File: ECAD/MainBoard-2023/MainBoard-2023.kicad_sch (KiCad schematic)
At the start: 71 parts, among them J1 XT60, J10 Conn_01x14, J11 Conn_01x03, J12 Conn_01x04, J13 Conn_01x03, J14 Conn_01x03, J15 Conn_01x03, J16 XT30, J17 XT30, J2 Conn_01x04, J20 BAU, J21 BAU, J22 Conn_01x04, J23 Conn_01x02, J24 Conn_01x07, J26 BAU, J27 BAU, J28 Conn_01x02, J29 Conn_01x02, J3 ConStep1, J30 Conn_01x03, J32 Conn_01x02, J37 Conn_01x02, J38 Conn_01x02, J39 Conn_01x02, J4 Conn_01x02, J40 Conn_01x02, J5 ConStep1, J6 ConStep1, J7 XT30, J8 Conn_01x02, J9 XT60, K1 CB1-P-24V, U1 Teensy3.5_All_Pins, U2 R-78B3.3-2.0, U4 R-78B5.0-2.0

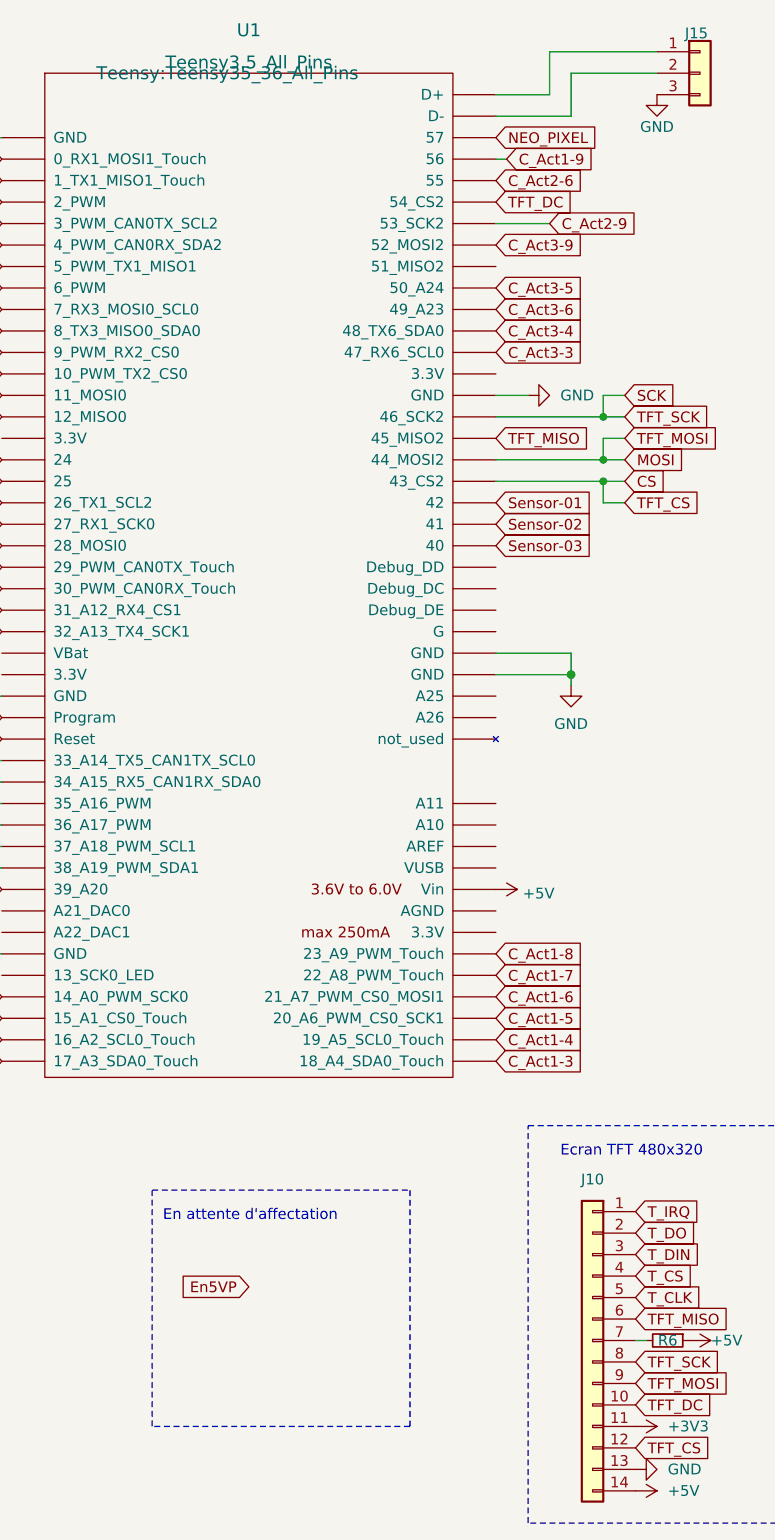
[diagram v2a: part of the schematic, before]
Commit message: clean PCB
Clean routing and DRC errors
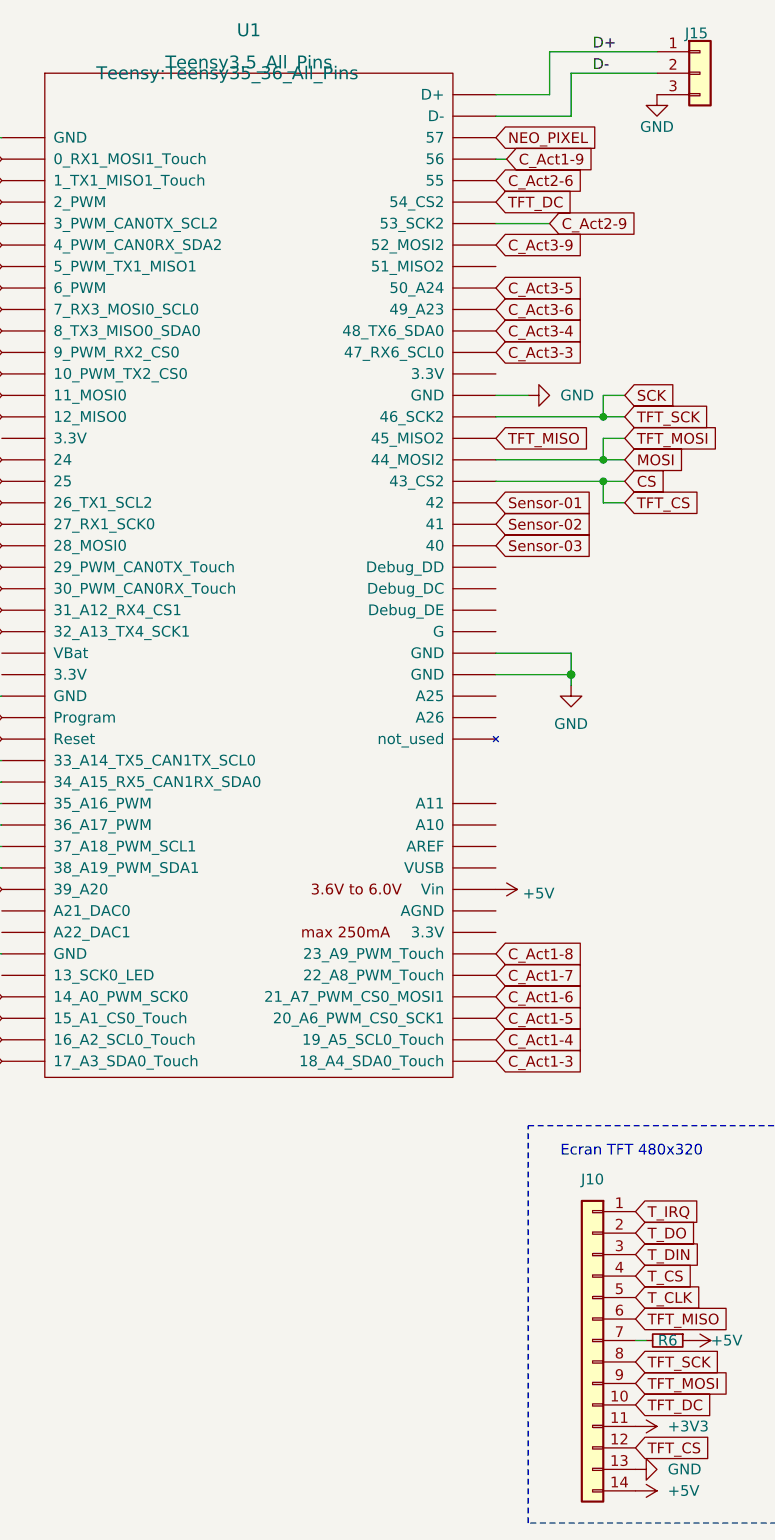
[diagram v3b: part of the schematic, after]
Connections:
- net D+: now reaches J15.1 (Pin_1), U1.88 (D+)
- net D-: now reaches J15.2 (Pin_2), U1.87 (D-)
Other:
- note removed: "En attente d'affectation"
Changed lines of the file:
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@@
     (stroke (width 0) (type default) (color 0 0 0 0))
-  )
-  (polyline (pts (xy 67.31 182.88) (xy 67.31 154.94))
-    (stroke (width 0) (type dash) (color 0 0 0 0))
   )
   (wire (pts (xy 195.58 125.73) (xy 199.39 125.73))
@@
     (stroke (width 0) (type dash) (color 0 0 0 0))
   )
-  (polyline (pts (xy 67.31 154.94) (xy 97.79 154.94))
-    (stroke (width 0) (type dash) (color 0 0 0 0))
-  )
   (polyline (pts (xy 143.51 165.1) (xy 143.51 137.16))
     (stroke (width 0) (type dash) (color 0 0 0 0))
@@
     (stroke (width 0) (type solid) (color 0 0 0 0))
   )
-  (polyline (pts (xy 97.79 154.94) (xy 97.79 182.88))
-    (stroke (width 0) (type dash) (color 0 0 0 0))
-  )
   (wire (pts (xy 123.19 71.12) (xy 120.65 71.12))
     (stroke (width 0) (type default) (color 0 0 0 0))
@@
   (wire (pts (xy 163.83 157.48) (xy 162.56 157.48))
     (stroke (width 0) (type default) (color 0 0 0 0))
-  )
-  (polyline (pts (xy 97.79 182.88) (xy 67.31 182.88))
-    (stroke (width 0) (type dash) (color 0 0 0 0))
   )
   (wire (pts (xy 191.77 149.86) (xy 194.31 149.86))
@@
     (effects (font (size 1 1)) (justify left bottom))
   )
-  (text "En attente d'affectation" (at 68.58 158.75 0)
-    (effects (font (size 1.27 1.27)) (justify left bottom))
-  )
   (text "Driver stepper" (at 233.68 20.32 0)
     (effects (font (size 1.27 1.27)) (justify left bottom))
@@
     (effects (font (size 1.27 1.27)) (justify left bottom))
   )
+  (label "D+" (at 119.38 20.32 0)
+    (effects (font (size 1.27 1.27)) (justify left bottom))
+  )
   (label "24VD" (at 172.72 149.86 0)
     (effects (font (size 1.27 1.27)) (justify left bottom))
   )
+  (label "D-" (at 119.38 22.86 0)
+    (effects (font (size 1.27 1.27)) (justify left bottom))
+  )
   (global_label "C_Act3-2" (shape input) (at 170.18 91.44 0) (fields_autoplaced)
     (effects (font (size 1.27 1.27)) (justify left))
@@
     )
   )
-  (global_label "En5VP" (shape input) (at 78.74 166.37 180) (fields_autoplaced)
-    (effects (font (size 1.27 1.27)) (justify right))
-    (property "Intersheet References" "${INTERSHEET_REFS}" (id 0) (at 70.4607 166.2906 0)
-      (effects (font (size 1.27 1.27)) (justify right) hide)
-    )
-  )

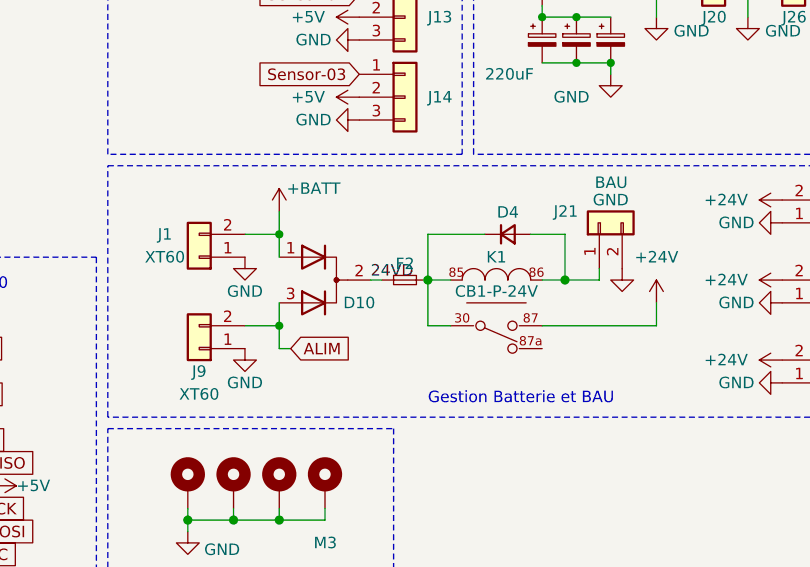
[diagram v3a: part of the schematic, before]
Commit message: Add silkscreen info
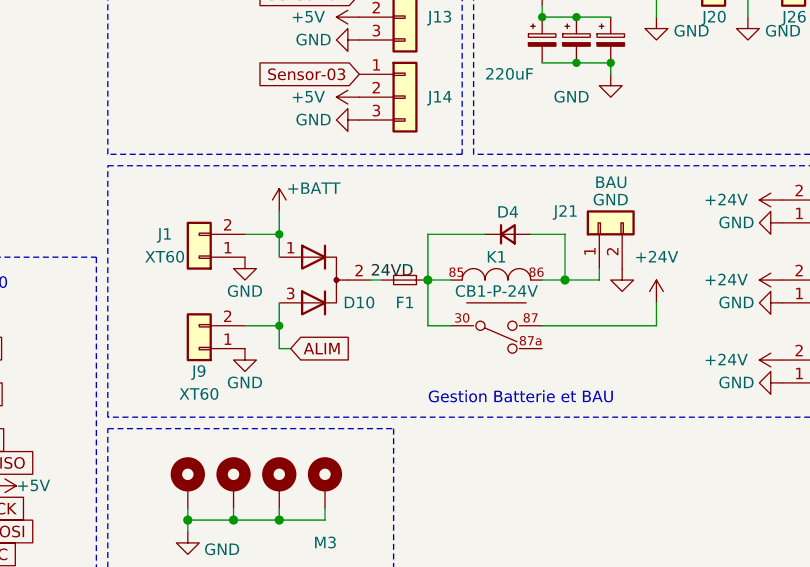
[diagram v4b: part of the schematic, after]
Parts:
- J16, J17, J7: footprint Connector_AMASS:AMASS_XT30UPB-F_1x02_P5.0mm_Vertical -> Connector_AMASS:AMASS_XT30U-F_1x02_P5.0mm_Vertical
- renumbered F2 to F1
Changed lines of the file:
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@@
     (property "Reference" "J17" (id 0) (at 223.52 163.83 0))
     (property "Value" "XT30" (id 1) (at 227.33 160.02 0))
-    (property "Footprint" "Connector_AMASS:AMASS_XT30UPB-F_1x02_P5.0mm_Vertical" (id 2) (at 223.52 161.29 0)
+    (property "Footprint" "Connector_AMASS:AMASS_XT30U-F_1x02_P5.0mm_Vertical" (id 2) (at 223.52 161.29 0)
       (effects (font (size 1.27 1.27)) hide)
     )
@@
   )
   (symbol (lib_id "Device:Fuse_Small") (at 176.53 149.86 0) (unit 1)
-    (in_bom yes) (on_board yes)
-    (property "Reference" "F2" (id 0) (at 176.53 148.0524 0))
+    (in_bom yes) (on_board yes) (fields_autoplaced)
+    (property "Reference" "F1" (id 0) (at 176.53 152.4 0))
     (property "Value" "Fuse_Small" (id 1) (at 174.7382 151.7401 0)
       (effects (font (size 1.27 1.27)) hide)
@@
     (property "Reference" "J7" (id 0) (at 223.52 146.05 0))
     (property "Value" "XT30" (id 1) (at 227.33 142.24 0))
-    (property "Footprint" "Connector_AMASS:AMASS_XT30UPB-F_1x02_P5.0mm_Vertical" (id 2) (at 223.52 143.51 0)
+    (property "Footprint" "Connector_AMASS:AMASS_XT30U-F_1x02_P5.0mm_Vertical" (id 2) (at 223.52 143.51 0)
       (effects (font (size 1.27 1.27)) hide)
     )
@@
     (property "Reference" "J16" (id 0) (at 223.52 154.94 0))
     (property "Value" "XT30" (id 1) (at 227.33 151.13 0))
-    (property "Footprint" "Connector_AMASS:AMASS_XT30UPB-F_1x02_P5.0mm_Vertical" (id 2) (at 223.52 152.4 0)
+    (property "Footprint" "Connector_AMASS:AMASS_XT30U-F_1x02_P5.0mm_Vertical" (id 2) (at 223.52 152.4 0)
       (effects (font (size 1.27 1.27)) hide)
     )
@@
     )
     (path "/7cfcbb01-03fd-4939-8bba-86c0cacd312b"
-      (reference "F2") (unit 1) (value "Fuse_Small") (footprint "Fuse:Fuseholder_Blade_Mini_Keystone_3568")
+      (reference "F1") (unit 1) (value "Fuse_Small") (footprint "Fuse:Fuseholder_Blade_Mini_Keystone_3568")
     )
     (path "/2ea04188-eb9b-4f84-b43b-9150de08bfa6"
@@
     )
     (path "/d607eb9a-23b4-4372-bc45-8aa1d6977fee"
-      (reference "J7") (unit 1) (value "XT30") (footprint "Connector_AMASS:AMASS_XT30UPB-F_1x02_P5.0mm_Vertical")
+      (reference "J7") (unit 1) (value "XT30") (footprint "Connector_AMASS:AMASS_XT30U-F_1x02_P5.0mm_Vertical")
     )
     (path "/48712099-d103-40ba-ac7d-d49154a7a9f3"
@@
     )
     (path "/f3434dd5-88d3-415d-862b-b58bbf14c1e6"
-      (reference "J16") (unit 1) (value "XT30") (footprint "Connector_AMASS:AMASS_XT30UPB-F_1x02_P5.0mm_Vertical")
+      (reference "J16") (unit 1) (value "XT30") (footprint "Connector_AMASS:AMASS_XT30U-F_1x02_P5.0mm_Vertical")
     )
     (path "/6fdadf38-3847-4a25-ae08-6e794881fa86"
-      (reference "J17") (unit 1) (value "XT30") (footprint "Connector_AMASS:AMASS_XT30UPB-F_1x02_P5.0mm_Vertical")
+      (reference "J17") (unit 1) (value "XT30") (footprint "Connector_AMASS:AMASS_XT30U-F_1x02_P5.0mm_Vertical")
     )
     (path "/8d2a78ab-0275-4a44-8c59-18e3f5a0f07e"

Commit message: Change Annotations
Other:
- company: (none) -> Les Karibous
- title: (none) -> Main Board 2023
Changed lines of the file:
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@@
 (kicad_sch (version 20211123) (generator eeschema)
   (paper "A4")
+  (title_block
+    (title "Main Board 2023")
+    (date "2022-08-08")
+    (rev "1")
+    (company "Les Karibous")
+  )
   (junction (at 194.31 59.69) (diameter 0) (color 0 0 0 0)
   )
